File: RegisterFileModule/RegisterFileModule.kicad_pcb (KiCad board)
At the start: 4 copper layers, 76.2 x 87.6 mm, 41 parts, among them J1 SelA, J2 SelB, J3 SelC, J4 Control Signals, J5 Y_WB, J6 StoreOp_WB, J7 RegisterA, J8 RegisterB, U1 74AHCT138, U2 74ABT16245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

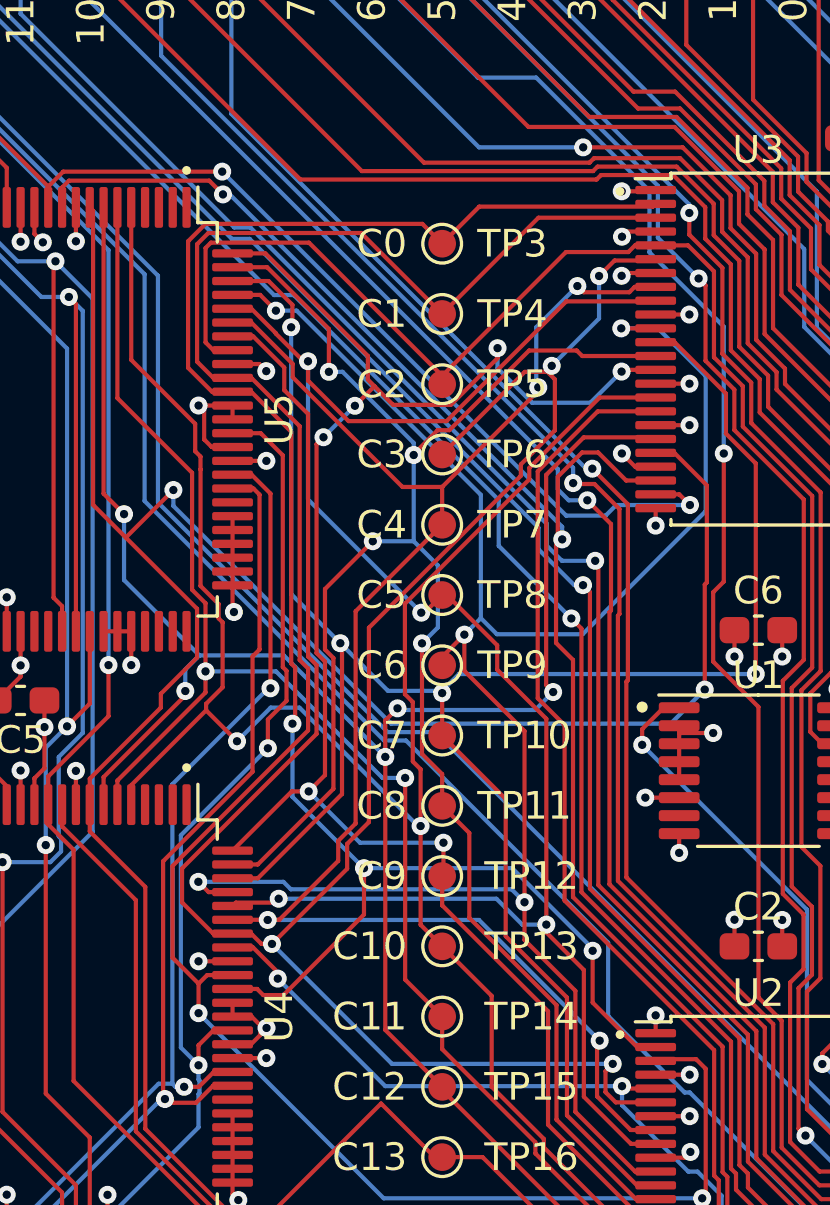
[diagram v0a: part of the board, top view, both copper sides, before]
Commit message: RegisterFileModule: update for KiCad 7
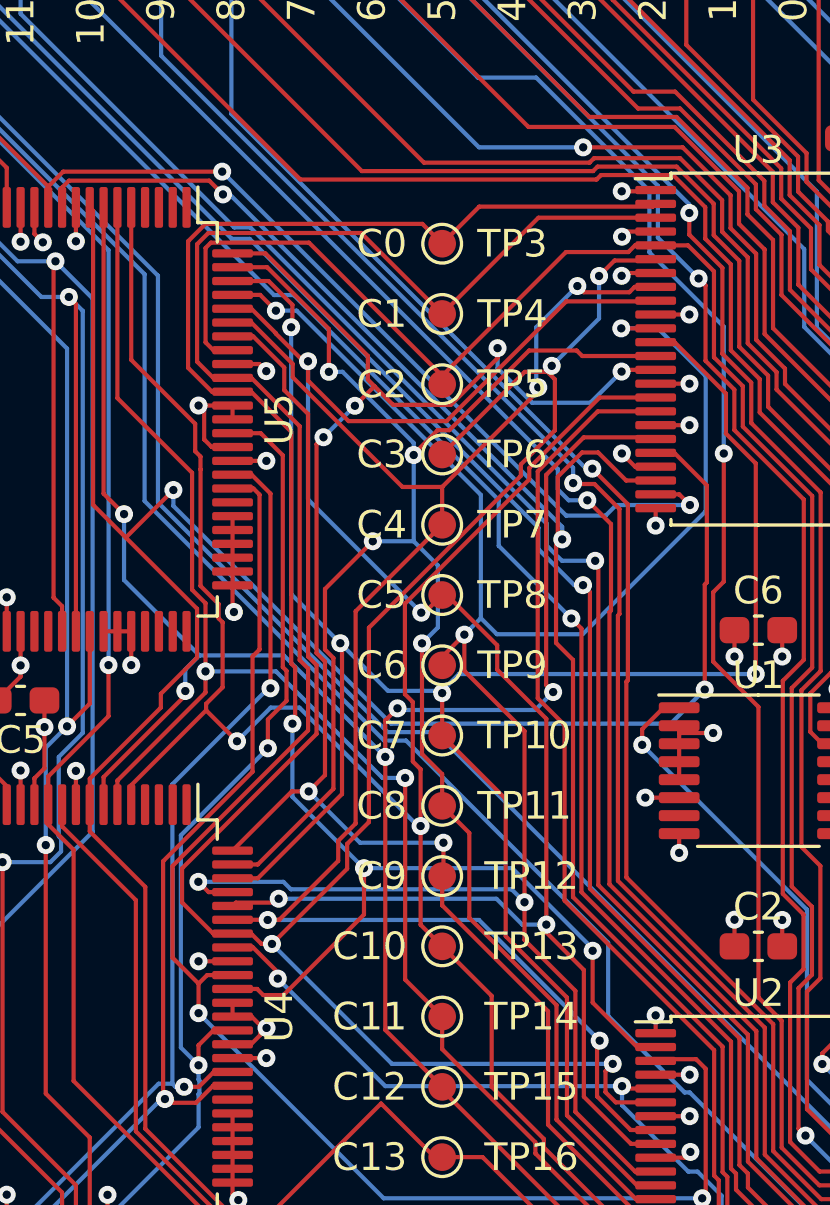
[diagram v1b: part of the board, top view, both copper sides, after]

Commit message: RegisterFileModule: Fix write-back timing bug
Fix the bug where the /WR signal to the SRAMs was arriving at an invalid
time. The signal arrival is now delayed by a series of logic gates. The
signal is deasserted before other inputs change by gating it against the
Phi2 clock.

Note that the main board schematic and PCB has not yet been updated.
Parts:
- added C5: 100nF, Capacitor_SMD:C_0603_1608Metric_Pad1.08x0.95mm_HandSolder, F.Cu at (144.8, 122.8)
- added J7: Phi2, Connector_PinHeader_2.54mm:PinHeader_1x02_P2.54mm_Vertical, F.Cu at (165.1, 138.4)
- added TP19: TP, TestPoint:TestPoint_Pad_D1.0mm, F.Cu at (151.1, 133.3)
- added TP20: TP, TestPoint:TestPoint_Pad_D1.0mm, F.Cu at (149.9, 120.7)
- added TP21: TP, TestPoint:TestPoint_Pad_D1.0mm, F.Cu at (154.9, 120.7)
- added TP22: TP, TestPoint:TestPoint_Pad_D1.0mm, F.Cu at (146.1, 133.3)
- added U4: 74AHCT32, Package_SO:TSSOP-14_4.4x5mm_P0.65mm, F.Cu at (149.1, 127.0)
- moved C7 28.3 mm to (163.6, 119.5), turned to 90 degrees
- moved U1 26.4 mm to (168.6, 122.9), turned to 90 degrees
- moved TP1 25.1 mm to (166.1, 115.2)
- moved TP2 18.9 mm to (171.2, 115.2)
- moved U2 10.6 mm to (170.8, 101.7), turned to 90 degrees
- moved C3 10.4 mm to (162.3, 78.7), turned to 90 degrees
- moved C2 7.88 mm to (162.3, 97.0), turned to 90 degrees
- moved U3 4.15 mm to (170.8, 83.9), turned to 90 degrees
- moved TP10 2.54 mm to (153.7, 95.2)
- moved TP11 2.54 mm to (153.7, 97.8)
- moved TP12 2.54 mm to (153.7, 100.3)
- moved TP13 2.54 mm to (153.7, 102.9)
- moved TP14 2.54 mm to (153.7, 105.4)
- moved TP15 2.54 mm to (153.7, 108.0)
- moved TP16 2.54 mm to (153.7, 110.5)
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- renumbered C5 to C6, C6 to C7, J7 to J8, J8 to J9, U4 to U5, U5 to U6
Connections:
- U5 pad 87: /Write Back and Register File/~{WBEN} -> /Write Back and Register File/sheet60693B95/~{WR}
- U6 pad 87: /Write Back and Register File/~{WBEN} -> /Write Back and Register File/sheet60693B95/~{WR}
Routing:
- net /Write Back and Register File/sheet60693B95/~{WR}: track 0.00 -> 60.9 mm, vias 0 -> 3
- net Net-(U1-O1): track 28.9 -> 60.7 mm, vias 0 -> 2
- net /Write Back and Register File/~{WBEN}: track 53.3 -> 22.3 mm, vias 2 -> 0
- net /Write Back and Register File/Select Write Back Source/C4: track 60.9 -> 91.5 mm, vias 4 -> 3
- net /Write Back and Register File/WriteBackSrc: track 72.0 -> 43.9 mm, vias 1 -> 0
- net /Write Back and Register File/Select Write Back Source/C5: track 66.3 -> 89.5 mm, vias 4 -> 0
- net /Write Back and Register File/Select Write Back Source/C1: track 81.0 -> 102.2 mm, vias 2 -> 3
- net /Write Back and Register File/Phi2: track 0.00 -> 19.0 mm
- net /Y_WB3: track 53.7 -> 35.1 mm
- net /Y_WB4: track 54.9 -> 36.3 mm
- net /Y_WB2: track 53.3 -> 35.6 mm
- net /SelC_WB0: track 81.7 -> 64.7 mm
- net /Y_WB7: track 56.9 -> 41.0 mm
- net /Write Back and Register File/Select Write Back Source/C8: track 68.4 -> 84.1 mm, vias 4 -> 3
- net /Y_WB6: track 54.8 -> 39.5 mm
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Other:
- board text added: "Turtle16: Write Back and Register File, Rev B Copyright © 2022-2023 Andrew Fox"
- board text removed: "Turtle16: Write Back and Register File, Rev A Copyright © 2022 Andrew Fox"

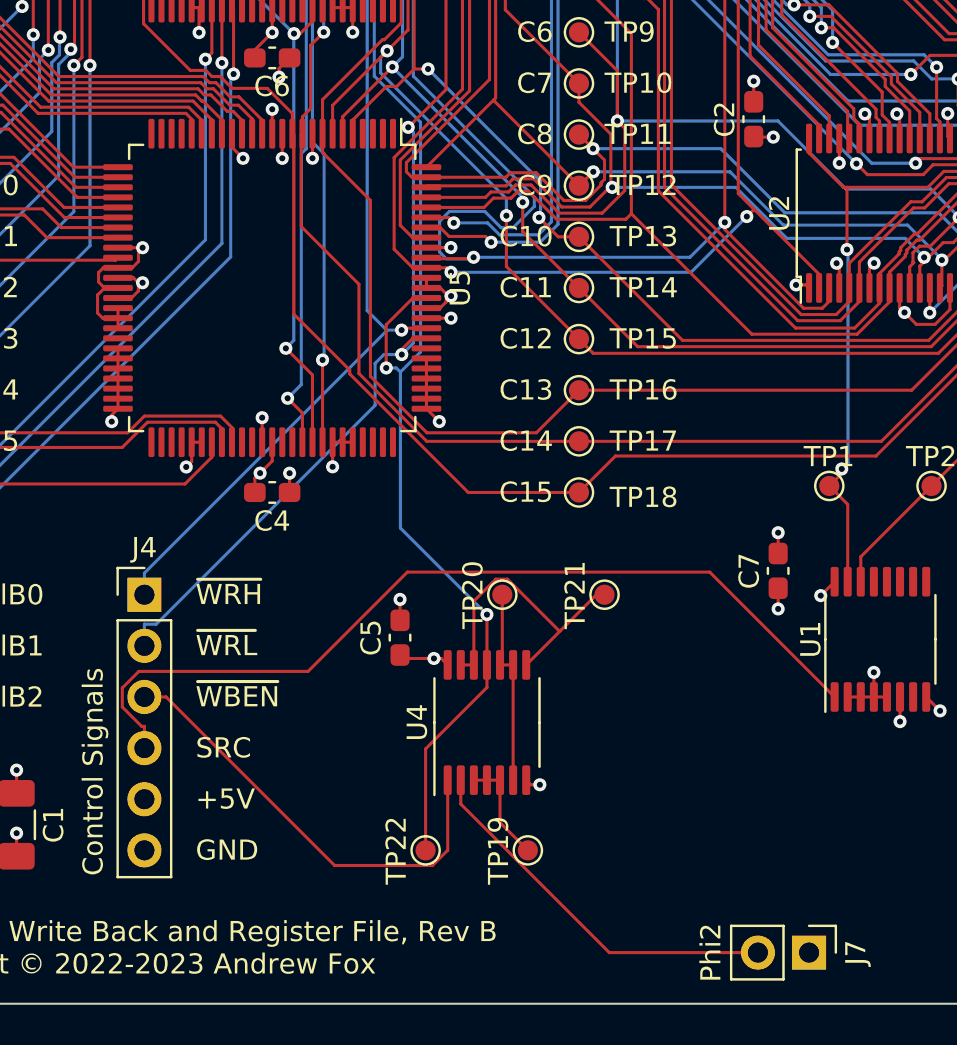
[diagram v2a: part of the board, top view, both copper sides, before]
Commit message: RegisterFileModule: Add jumpers to make it easier to experiment with delay.
Easily cut and solder jumpers to select the delay to use on the WR signal.
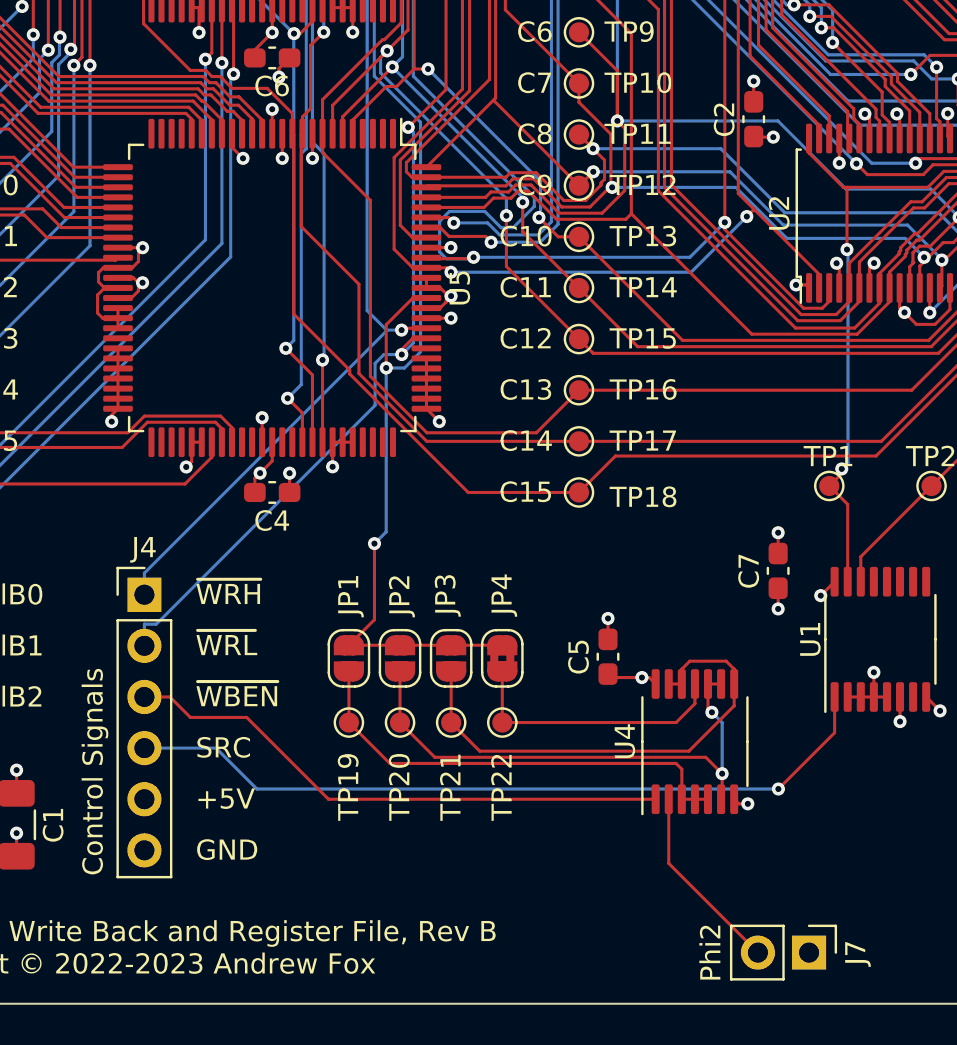
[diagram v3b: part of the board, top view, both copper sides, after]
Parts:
- added JP1: SolderJumper_2_Open, Jumper:SolderJumper-2_P1.3mm_Open_RoundedPad1.0x1.5mm, F.Cu at (142.2, 123.8)
- added JP2: SolderJumper_2_Open, Jumper:SolderJumper-2_P1.3mm_Open_RoundedPad1.0x1.5mm, F.Cu at (144.8, 123.8)
- added JP3: SolderJumper_2_Open, Jumper:SolderJumper-2_P1.3mm_Open_RoundedPad1.0x1.5mm, F.Cu at (147.3, 123.8)
- added JP4: SolderJumper_2_Bridged, Jumper:SolderJumper-2_P1.3mm_Bridged2Bar_RoundedPad1.0x1.5mm, F.Cu at (149.9, 123.8)
- moved TP19 10.9 mm to (142.2, 127.0)
- moved C5 10.4 mm to (155.1, 123.7)
- moved U4 10.4 mm to (159.4, 127.9)
- moved TP21 9.92 mm to (147.3, 127.0)
- moved TP20 8.13 mm to (144.8, 127.0)
- moved TP22 7.41 mm to (149.9, 127.0)
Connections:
- TP22 pad 1: /Write Back and Register File/sheet60693B95/~{WR} -> Net-(JP4-A)
- U4 pad 11: /Write Back and Register File/sheet60693B95/~{WR} -> Net-(JP4-A)
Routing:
- net Net-(JP1-A): track 5.36 -> 22.8 mm
- net Net-(JP2-A): track 9.86 -> 26.3 mm, vias 0 -> 2
- net Net-(JP4-A): track 0.00 -> 13.5 mm
- net /Write Back and Register File/Phi2: track 19.0 -> 9.45 mm
- net Net-(JP3-A): track 15.0 -> 24.3 mm
- net /Write Back and Register File/WriteBackSrc: track 43.9 -> 38.1 mm, vias 0 -> 1
- net /Write Back and Register File/~{WBEN}: track 22.3 -> 27.5 mm
- net /Write Back and Register File/sheet60693B95/~{WR}: track 60.9 -> 56.1 mm
